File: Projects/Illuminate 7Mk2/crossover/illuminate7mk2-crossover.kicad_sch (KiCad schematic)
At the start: 23 parts, among them J1 IN (amp), J2 TWEETER, J3 WOOFER

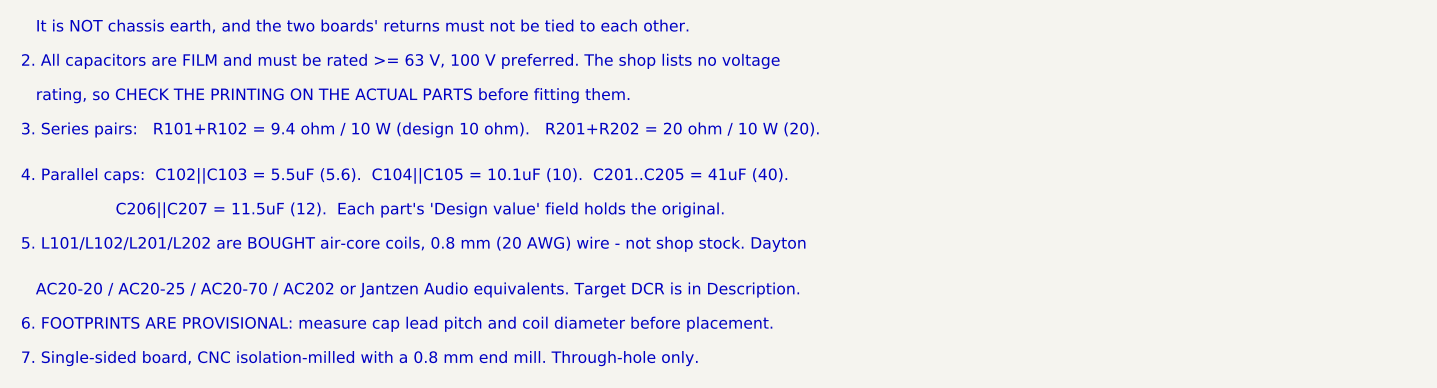
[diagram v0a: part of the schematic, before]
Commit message: Illuminate 7Mk2: crossover board shrunk to the mill envelope
Coils moved off the board: only their lead pads remain, at the edges.
Board is now 167 x 144 mm, inside the 203 x 152 mm build size.
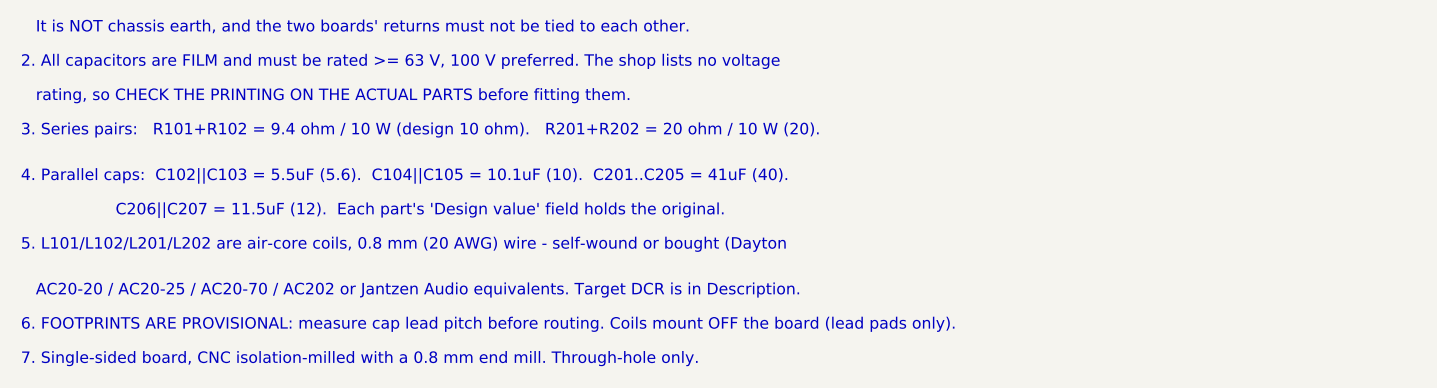
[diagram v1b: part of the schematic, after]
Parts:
- L101: footprint crossover:L_AirCore_D40mm_0.8mm -> crossover:L_OffBoard_P10.16mm
- L102: footprint crossover:L_AirCore_D42mm_0.8mm -> crossover:L_OffBoard_P10.16mm
- L201: footprint crossover:L_AirCore_D55mm_0.8mm -> crossover:L_OffBoard_P10.16mm
- L202: footprint crossover:L_AirCore_D70mm_0.8mm -> crossover:L_OffBoard_P10.16mm
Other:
- note added: "5. L101/L102/L201/L202 are air-core coils, 0.8 mm (20 AWG) wire - self-wound or bought (Dayton"
- note added: "6. FOOTPRINTS ARE PROVISIONAL: measure cap lead pitch before routing. Coils mount OFF the board (lead pads only)."
- note removed: "5. L101/L102/L201/L202 are BOUGHT air-core coils, 0.8 mm (20 AWG) wire - not shop stock. Dayton"
- note removed: "6. FOOTPRINTS ARE PROVISIONAL: measure cap lead pitch and coil diameter before placement."
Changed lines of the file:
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@@
 		)
 	)
-	(text "5. L101/L102/L201/L202 are BOUGHT air-core coils, 0.8 mm (20 AWG) wire - not shop stock. Dayton"
+	(text "5. L101/L102/L201/L202 are air-core coils, 0.8 mm (20 AWG) wire - self-wound or bought (Dayton"
 		(at 12.7 179.07 0)
 		(effects
@@
 		)
 	)
-	(text "6. FOOTPRINTS ARE PROVISIONAL: measure cap lead pitch and coil diameter before placement."
+	(text "6. FOOTPRINTS ARE PROVISIONAL: measure cap lead pitch before routing. Coils mount OFF the board (lead pads only)."
 		(at 12.7 187.96 0)
 		(effects
@@
 			)
 		)
-		(property "Footprint" "crossover:L_AirCore_D40mm_0.8mm"
+		(property "Footprint" "crossover:L_OffBoard_P10.16mm"
 			(at 69.85 40.64 0)
 			(hide yes)
@@
 			)
 		)
-		(property "Footprint" "crossover:L_AirCore_D42mm_0.8mm"
+		(property "Footprint" "crossover:L_OffBoard_P10.16mm"
 			(at 147.32 60.96 0)
 			(hide yes)
@@
 			)
 		)
-		(property "Footprint" "crossover:L_AirCore_D55mm_0.8mm"
+		(property "Footprint" "crossover:L_OffBoard_P10.16mm"
 			(at 81.28 119.38 0)
 			(hide yes)
@@
 			)
 		)
-		(property "Footprint" "crossover:L_AirCore_D70mm_0.8mm"
+		(property "Footprint" "crossover:L_OffBoard_P10.16mm"
 			(at 154.94 119.38 0)
 			(hide yes)

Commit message: Illuminate 7Mk2: crossover re-placed on measured shop-part footprints
All film caps, 5 W resistors and the screw terminal were measured on the
DTU shop parts and given matching stock footprints. The board re-packs to
151 x 120 mm; pcb_build.py now drops the bottom edge so the corner holes
clear every courtyard. README, handoff and BOM updated.
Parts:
- C101, C103: footprint Capacitor_THT:C_Rect_L29.0mm_W13.0mm_P27.50mm_MKT -> Capacitor_THT:C_Rect_L26.5mm_W7.0mm_P22.50mm_MKS4
- C102, C105, C207: footprint Capacitor_THT:C_Rect_L29.0mm_W13.0mm_P27.50mm_MKT -> Capacitor_THT:C_Rect_L26.5mm_W8.5mm_P22.50mm_MKS4
- C104: footprint Capacitor_THT:C_Rect_L41.5mm_W20.0mm_P37.50mm_MKS4 -> Capacitor_THT:C_Rect_L31.5mm_W11.0mm_P27.50mm_MKS4
- C201, C202, C203, C204, C205, C206: footprint Capacitor_THT:C_Rect_L41.5mm_W20.0mm_P37.50mm_MKS4 -> Capacitor_THT:C_Rect_L31.5mm_W13.0mm_P27.50mm_MKS4
- R101, R102: footprint Resistor_THT:R_Axial_Power_L25.0mm_W9.0mm_P30.48mm -> Resistor_THT:R_Axial_Power_L25.0mm_W9.0mm_P27.94mm
- R201, R202: footprint Resistor_THT:R_Axial_Power_L25.0mm_W9.0mm_P30.48mm -> Resistor_THT:R_Axial_Power_L20.0mm_W6.4mm_P22.40mm
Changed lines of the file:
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@@
 			)
 		)
-		(property "Footprint" "Capacitor_THT:C_Rect_L29.0mm_W13.0mm_P27.50mm_MKT"
+		(property "Footprint" "Capacitor_THT:C_Rect_L26.5mm_W7.0mm_P22.50mm_MKS4"
 			(at 69.85 27.94 0)
 			(hide yes)
@@
 			)
 		)
-		(property "Footprint" "Resistor_THT:R_Axial_Power_L25.0mm_W9.0mm_P30.48mm"
+		(property "Footprint" "Resistor_THT:R_Axial_Power_L25.0mm_W9.0mm_P27.94mm"
 			(at 59.69 53.34 0)
 			(hide yes)
@@
 			)
 		)
-		(property "Footprint" "Resistor_THT:R_Axial_Power_L25.0mm_W9.0mm_P30.48mm"
+		(property "Footprint" "Resistor_THT:R_Axial_Power_L25.0mm_W9.0mm_P27.94mm"
 			(at 80.01 53.34 0)
 			(hide yes)
@@
 			)
 		)
-		(property "Footprint" "Capacitor_THT:C_Rect_L29.0mm_W13.0mm_P27.50mm_MKT"
+		(property "Footprint" "Capacitor_THT:C_Rect_L26.5mm_W8.5mm_P22.50mm_MKS4"
 			(at 119.38 33.02 0)
 			(hide yes)
@@
 			)
 		)
-		(property "Footprint" "Capacitor_THT:C_Rect_L29.0mm_W13.0mm_P27.50mm_MKT"
+		(property "Footprint" "Capacitor_THT:C_Rect_L26.5mm_W7.0mm_P22.50mm_MKS4"
 			(at 119.38 48.26 0)
 			(hide yes)
@@
 			)
 		)
-		(property "Footprint" "Capacitor_THT:C_Rect_L41.5mm_W20.0mm_P37.50mm_MKS4"
+		(property "Footprint" "Capacitor_THT:C_Rect_L31.5mm_W11.0mm_P27.50mm_MKS4"
 			(at 175.26 33.02 0)
 			(hide yes)
@@
 			)
 		)
-		(property "Footprint" "Capacitor_THT:C_Rect_L29.0mm_W13.0mm_P27.50mm_MKT"
+		(property "Footprint" "Capacitor_THT:C_Rect_L26.5mm_W8.5mm_P22.50mm_MKS4"
 			(at 175.26 48.26 0)
 			(hide yes)
@@
 			)
 		)
-		(property "Footprint" "Capacitor_THT:C_Rect_L41.5mm_W20.0mm_P37.50mm_MKS4"
+		(property "Footprint" "Capacitor_THT:C_Rect_L31.5mm_W13.0mm_P27.50mm_MKS4"
 			(at 58.42 107.95 0)
 			(hide yes)
@@
 			)
 		)
-		(property "Footprint" "Capacitor_THT:C_Rect_L41.5mm_W20.0mm_P37.50mm_MKS4"
+		(property "Footprint" "Capacitor_THT:C_Rect_L31.5mm_W13.0mm_P27.50mm_MKS4"
 			(at 71.12 107.95 0)
 			(hide yes)
@@
 			)
 		)
-		(property "Footprint" "Capacitor_THT:C_Rect_L41.5mm_W20.0mm_P37.50mm_MKS4"
+		(property "Footprint" "Capacitor_THT:C_Rect_L31.5mm_W13.0mm_P27.50mm_MKS4"
 			(at 83.82 107.95 0)
 			(hide yes)
@@
 			)
 		)
-		(property "Footprint" "Capacitor_THT:C_Rect_L41.5mm_W20.0mm_P37.50mm_MKS4"
+		(property "Footprint" "Capacitor_THT:C_Rect_L31.5mm_W13.0mm_P27.50mm_MKS4"
 			(at 96.52 107.95 0)
 			(hide yes)
@@
 			)
 		)
-		(property "Footprint" "Capacitor_THT:C_Rect_L41.5mm_W20.0mm_P37.50mm_MKS4"
+		(property "Footprint" "Capacitor_THT:C_Rect_L31.5mm_W13.0mm_P27.50mm_MKS4"
 			(at 109.22 107.95 0)
 			(hide yes)
@@
 			)
 		)
-		(property "Footprint" "Resistor_THT:R_Axial_Power_L25.0mm_W9.0mm_P30.48mm"
+		(property "Footprint" "Resistor_THT:R_Axial_Power_L20.0mm_W6.4mm_P22.40mm"
 			(at 71.12 132.08 0)
 			(hide yes)
@@
 			)
 		)
-		(property "Footprint" "Resistor_THT:R_Axial_Power_L25.0mm_W9.0mm_P30.48mm"
+		(property "Footprint" "Resistor_THT:R_Axial_Power_L20.0mm_W6.4mm_P22.40mm"
 			(at 91.44 132.08 0)
 			(hide yes)
@@
 			)
 		)
-		(property "Footprint" "Capacitor_THT:C_Rect_L41.5mm_W20.0mm_P37.50mm_MKS4"
+		(property "Footprint" "Capacitor_THT:C_Rect_L31.5mm_W13.0mm_P27.50mm_MKS4"
 			(at 187.96 133.35 0)
 			(hide yes)
@@
 			)
 		)
-		(property "Footprint" "Capacitor_THT:C_Rect_L29.0mm_W13.0mm_P27.50mm_MKT"
+		(property "Footprint" "Capacitor_THT:C_Rect_L26.5mm_W8.5mm_P22.50mm_MKS4"
 			(at 203.2 133.35 0)
 			(hide yes)
